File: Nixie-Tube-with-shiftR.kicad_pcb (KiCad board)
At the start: 2 copper layers, 37 x 53.3 mm, 55 parts, among them J1 Conn_01x06_Male, J2 Conn_01x01_Female, J3 Conn_01x06_Female, J4 Conn_01x01_Male, Q1 MMBTA42LT1, Q10 MMBTA42LT1, Q11 AO3400, Q12 AO3400, Q13 AO3400, Q14 MMBTA42LT1, Q15 MMBTA42LT1, Q2 MMBTA42LT1, Q3 MMBTA42LT1, Q4 MMBTA42LT1, Q5 MMBTA42LT1, Q6 MMBTA42LT1, Q7 MMBTA42LT1, Q8 MMBTA42LT1, Q9 MMBTA42LT1, U1 74HC595D, U2 nixie-tube, U3 74HC595D, U4 ams1117-5.0

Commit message: adjusted dimension on the 4 m3 holes
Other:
- board text removed: "6mm pin to bottom"
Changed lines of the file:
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@@
   (general
     (links 106)
-    (no_connects 2)
-    (area 149.233333 42.175 199.225239 92.075001)
+    (no_connects 0)
+    (area 140.149644 39.875 199.225239 100.100001)
     (thickness 1.6)
-    (drawings 15)
+    (drawings 14)
     (tracks 887)
     (zones 0)
@@
     (add_net +9V)
   )
+  (module Capacitors_SMD:C_0603 (layer B.Cu)
+    (at 182.5 72.5)
+    (descr "Capacitor SMD 0603, reflow soldering, AVX (see smccp.pdf)")
+    (tags "capacitor 0603")
+    (attr smd)
+    (fp_text reference C2 (at 0 1.5) (layer B.SilkS)
+      (effects (font (size 1 1) (thickness 0.15)) (justify mirror))
+    )
+    (fp_text value 10uF (at 0 -1.5) (layer B.Fab)
+      (effects (font (size 1 1) (thickness 0.15)) (justify mirror))
+    )
+    (fp_line (start 1.4 -0.65) (end -1.4 -0.65) (layer B.CrtYd) (width 0.05))
+    (fp_line (start 1.4 -0.65) (end 1.4 0.65) (layer B.CrtYd) (width 0.05))
+    (fp_line (start -1.4 0.65) (end -1.4 -0.65) (layer B.CrtYd) (width 0.05))
+    (fp_line (start -1.4 0.65) (end 1.4 0.65) (layer B.CrtYd) (width 0.05))
+    (fp_line (start 0.35 -0.6) (end -0.35 -0.6) (layer B.SilkS) (width 0.12))
+    (fp_line (start -0.35 0.6) (end 0.35 0.6) (layer B.SilkS) (width 0.12))
+    (fp_line (start -0.8 0.4) (end 0.8 0.4) (layer B.Fab) (width 0.1))
+    (fp_line (start 0.8 0.4) (end 0.8 -0.4) (layer B.Fab) (width 0.1))
+    (fp_line (start 0.8 -0.4) (end -0.8 -0.4) (layer B.Fab) (width 0.1))
+    (fp_line (start -0.8 -0.4) (end -0.8 0.4) (layer B.Fab) (width 0.1))
+    (fp_text user %R (at 0 0) (layer B.Fab)
+      (effects (font (size 0.3 0.3) (thickness 0.075)) (justify mirror))
+    )
+    (pad 2 smd rect (at 0.75 0) (size 0.8 0.75) (layers B.Cu B.Paste B.Mask)
+      (net 1 GND))
+    (pad 1 smd rect (at -0.75 0) (size 0.8 0.75) (layers B.Cu B.Paste B.Mask)
+      (net 3 +5V))
+    (model Capacitors_SMD.3dshapes/C_0603.wrl
+      (at (xyz 0 0 0))
+      (scale (xyz 1 1 1))
+      (rotate (xyz 0 0 0))
+    )
+  )
   (module TO_SOT_Packages_SMD:SOT-223-3Lead_TabPin2 (layer F.Cu)
     (at 157.075 82.85 270)
@@
   )
   (module Capacitors_SMD:C_0603 (layer B.Cu)
-    (at 182.5 72.5)
-    (descr "Capacitor SMD 0603, reflow soldering, AVX (see smccp.pdf)")
-    (tags "capacitor 0603")
-    (attr smd)
-    (fp_text reference C2 (at 0 1.5) (layer B.SilkS)
-      (effects (font (size 1 1) (thickness 0.15)) (justify mirror))
-    )
-    (fp_text value 10uF (at 0 -1.5) (layer B.Fab)
-      (effects (font (size 1 1) (thickness 0.15)) (justify mirror))
-    )
-    (fp_line (start 1.4 -0.65) (end -1.4 -0.65) (layer B.CrtYd) (width 0.05))
-    (fp_line (start 1.4 -0.65) (end 1.4 0.65) (layer B.CrtYd) (width 0.05))
-    (fp_line (start -1.4 0.65) (end -1.4 -0.65) (layer B.CrtYd) (width 0.05))
-    (fp_line (start -1.4 0.65) (end 1.4 0.65) (layer B.CrtYd) (width 0.05))
-    (fp_line (start 0.35 -0.6) (end -0.35 -0.6) (layer B.SilkS) (width 0.12))
-    (fp_line (start -0.35 0.6) (end 0.35 0.6) (layer B.SilkS) (width 0.12))
-    (fp_line (start -0.8 0.4) (end 0.8 0.4) (layer B.Fab) (width 0.1))
-    (fp_line (start 0.8 0.4) (end 0.8 -0.4) (layer B.Fab) (width 0.1))
-    (fp_line (start 0.8 -0.4) (end -0.8 -0.4) (layer B.Fab) (width 0.1))
-    (fp_line (start -0.8 -0.4) (end -0.8 0.4) (layer B.Fab) (width 0.1))
-    (fp_text user %R (at 0 0) (layer B.Fab)
-      (effects (font (size 0.3 0.3) (thickness 0.075)) (justify mirror))
-    )
-    (pad 2 smd rect (at 0.75 0) (size 0.8 0.75) (layers B.Cu B.Paste B.Mask)
-      (net 1 GND))
-    (pad 1 smd rect (at -0.75 0) (size 0.8 0.75) (layers B.Cu B.Paste B.Mask)
-      (net 3 +5V))
-    (model Capacitors_SMD.3dshapes/C_0603.wrl
-      (at (xyz 0 0 0))
-      (scale (xyz 1 1 1))
-      (rotate (xyz 0 0 0))
-    )
-  )
-  (module Capacitors_SMD:C_0603 (layer B.Cu)
     (at 182.5 74.65 180)
     (descr "Capacitor SMD 0603, reflow soldering, AVX (see smccp.pdf)")
@@
     (effects (font (size 0.5 0.5) (thickness 0.1)))
   )
-  (gr_text "6mm\n pin to bottom" (at 192 92.1) (layer Eco1.User)
-    (effects (font (size 0.5 0.5) (thickness 0.1)))
-  )

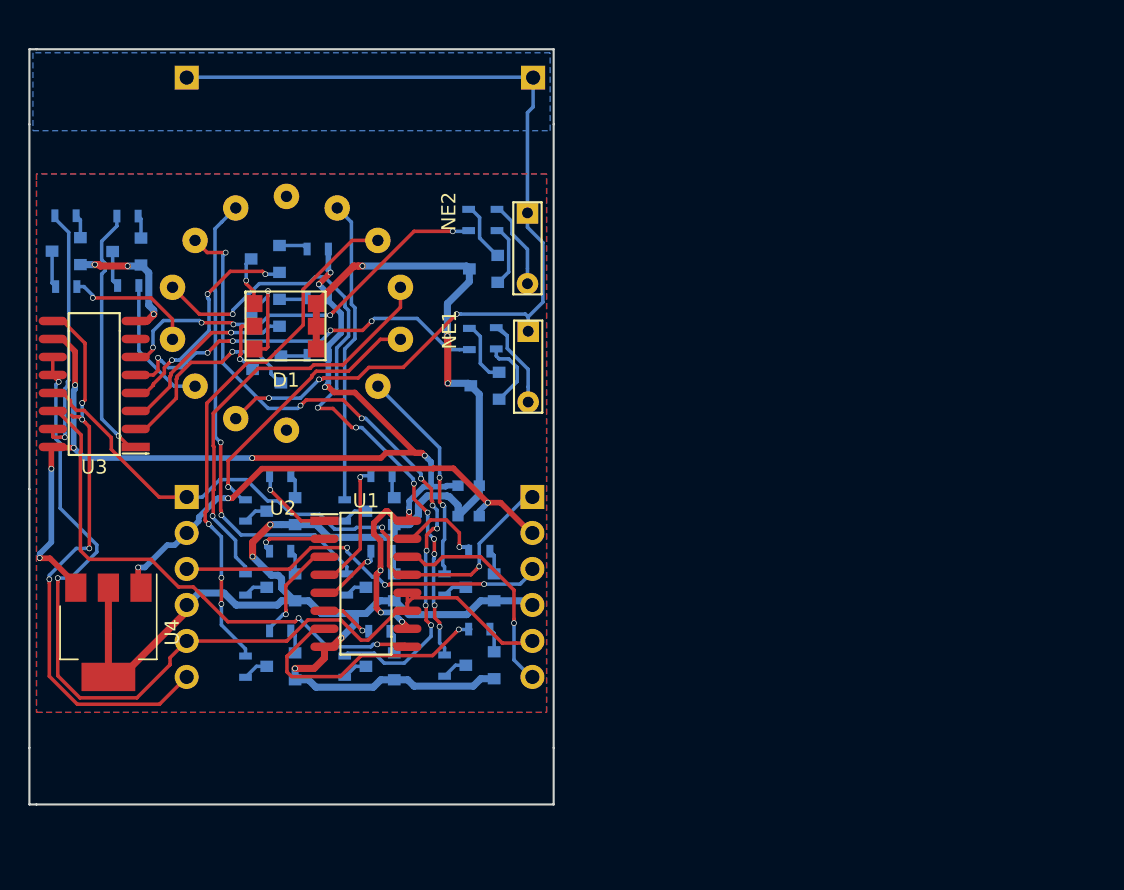
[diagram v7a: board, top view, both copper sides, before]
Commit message: added 4 m3 holes
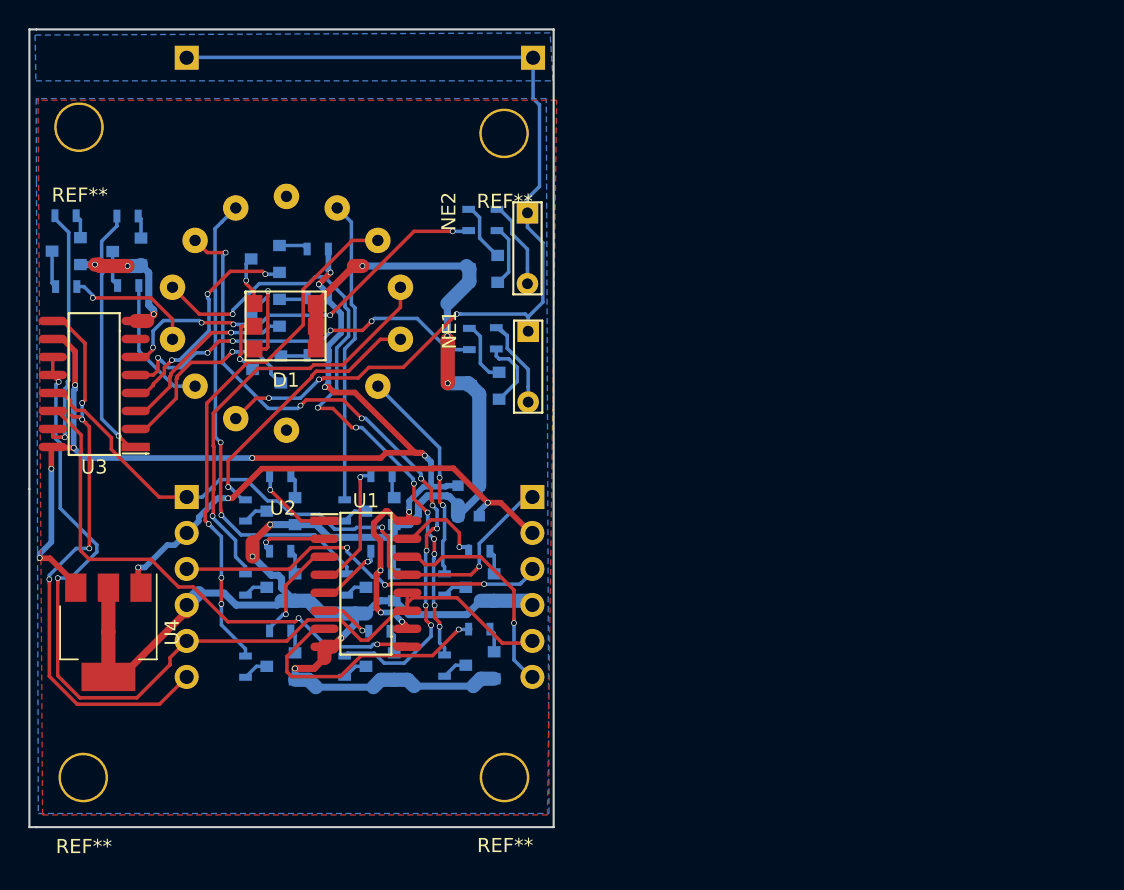
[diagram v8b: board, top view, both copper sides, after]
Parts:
- added REF**: mountingHole, nixie-tube-fp:mountingHole, F.Cu at (185.0, 93.1)
- added REF**: mountingHole, nixie-tube-fp:mountingHole, F.Cu at (155.3, 93.2)
- added REF**: mountingHole, nixie-tube-fp:mountingHole, F.Cu at (155.0, 47.2)
- added REF**: mountingHole, nixie-tube-fp:mountingHole, F.Cu at (185.0, 47.6)
- moved J2 1.40 mm to (187.1, 42.3)
- moved J4 1.40 mm to (162.6, 42.3)
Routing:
- net Net-(J2-Pad1): track 66.6 -> 68.4 mm
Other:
- board size 37 x 53.3 mm -> 37 x 56.3 mm
- net class GND: trace_width 0.5 -> 1
